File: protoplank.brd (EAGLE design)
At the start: 80 x 49 mm, 110 parts, among them IC1 74AHC1G86DBV

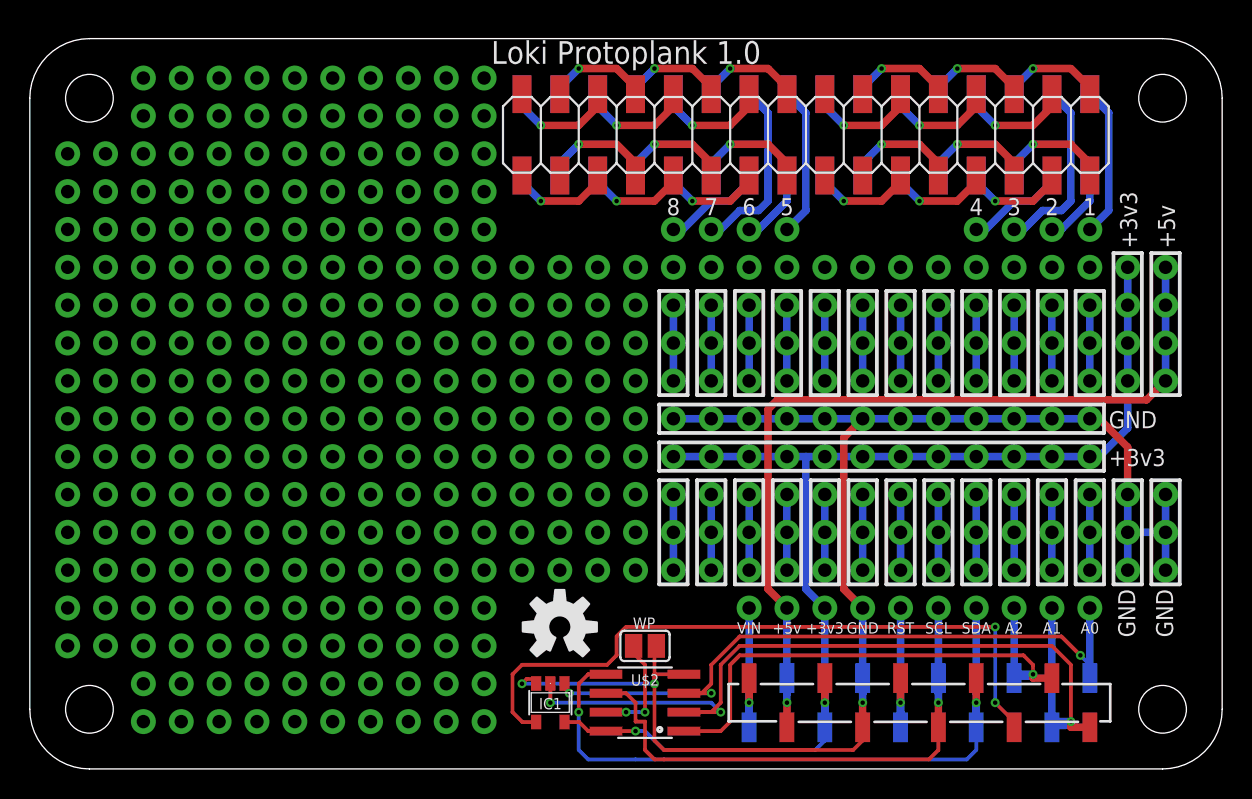
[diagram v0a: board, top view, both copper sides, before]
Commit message: Updated protoplank to use square pads for ease of SMT soldering.
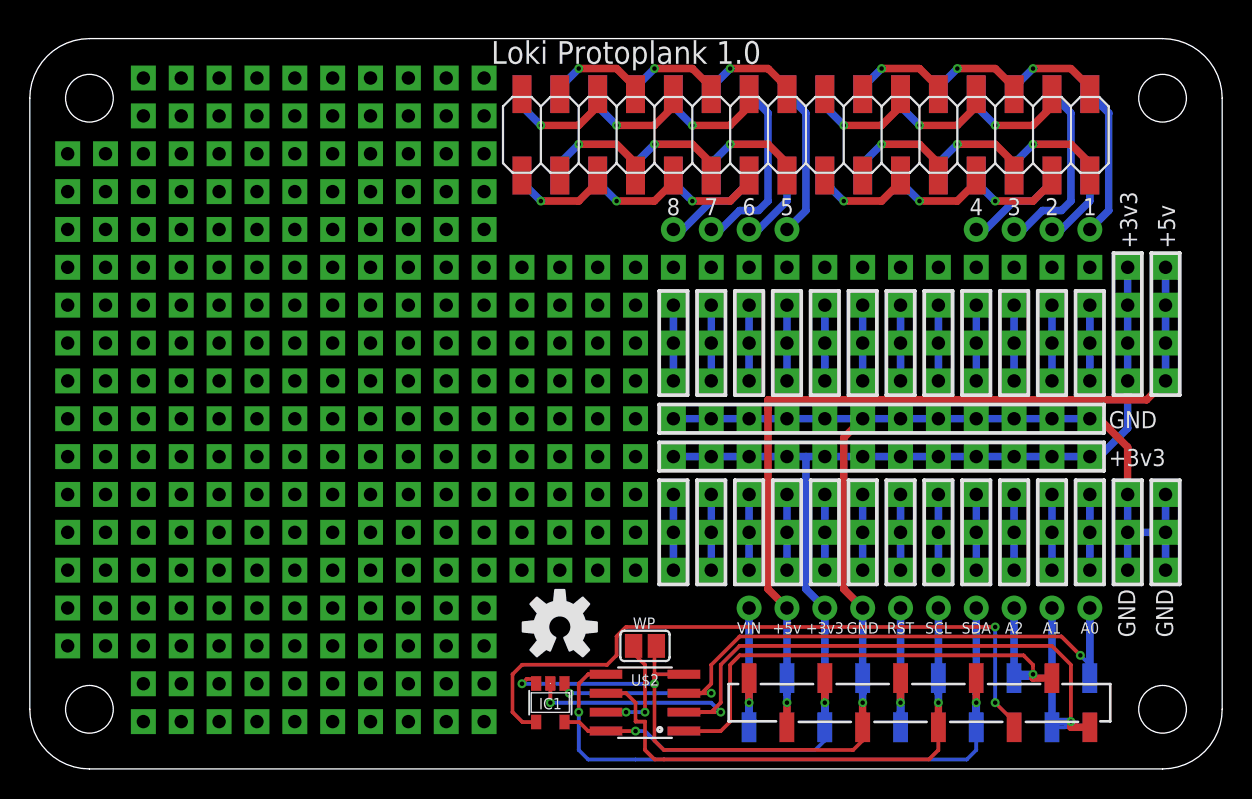
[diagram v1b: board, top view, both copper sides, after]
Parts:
- U$100, U$101, U$102, U$103, U$23, U$24, U$25, U$26, U$34, U$35, U$36, U$37, U$38, U$39, U$40, U$41, U$42, U$43, U$44, U$45, U$46, U$47, U$48, U$49, U$50, U$51, U$52, U$53, U$54, U$55, U$56, U$57, U$58, U$59, U$60, U$61, U$62, U$63, U$64, U$65, U$66, U$67, U$68, U$69, U$70, U$71, U$72, U$73, U$74, U$75, U$76, U$77, U$79, U$81, U$82, U$83, U$84, U$85, U$86, U$87, U$88, U$89, U$90, U$91, U$92, U$93, U$94, U$95, U$96, U$97, U$98, U$99: value PROTOPAD-4 -> PROTOPAD-4SQUARE
- U$104, U$105, U$106, U$107, U$27, U$28: value PROTOPAD-2 -> PROTOPAD-2SQUARE
- U$29, U$30, U$31, U$32: value PROTOPAD-4 -> PROTOPAD-4ROUND; device nickparts:PROTOPAD-4 -> nickparts:PROTOPAD-4-ROUND
- U$33: value PROTOPAD-2 -> PROTOPAD-2ROUND; device nickparts:PROTOPAD-2 -> nickparts:PROTOPAD-2-ROUND

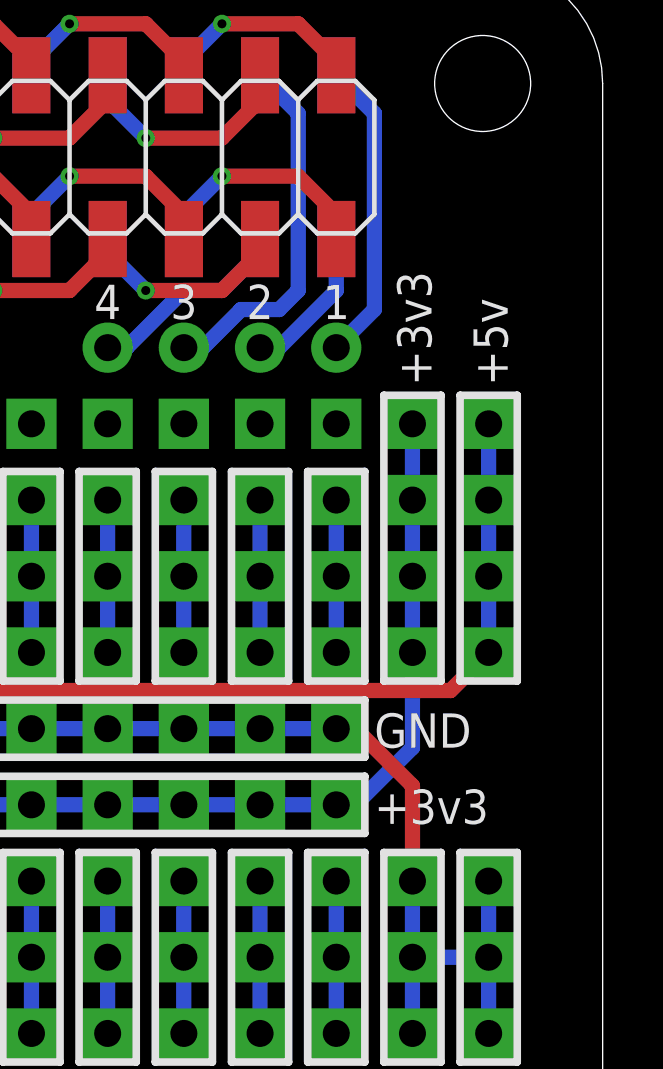
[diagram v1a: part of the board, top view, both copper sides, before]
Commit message: Added decoupling capacitors to the protoboard.
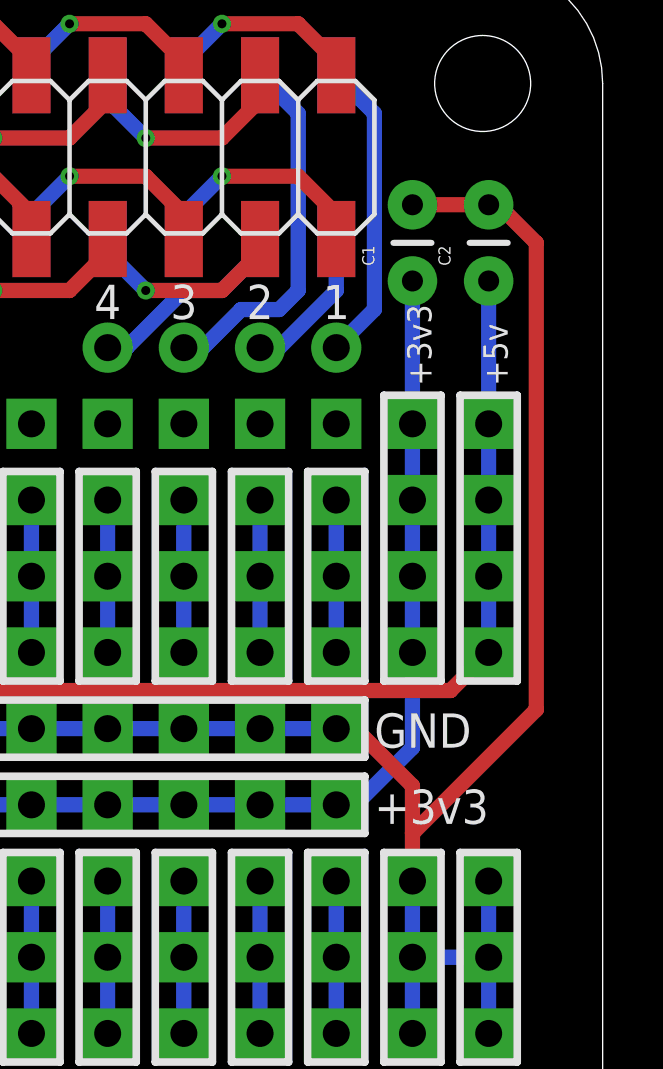
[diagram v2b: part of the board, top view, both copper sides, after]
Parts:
- added C1, C2: (no value), SparkFun-Passives:CAP-PTH-SMALL
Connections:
- net +3V3: now also C1.1
- net +5V: now also C2.1
- net GND: now also C1.2, C2.2
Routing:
- net GND: track 105.3 -> 131.3 mm
- net +3V3: track 82.4 -> 87.2 mm
- net +5V: track 58.3 -> 63.1 mm
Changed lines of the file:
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@@
 <text x="73.66" y="22.86" size="1.143" layer="21">GND</text>
 <text x="73.66" y="20.32" size="1.143" layer="21">+3v3</text>
-<text x="75.565" y="34.925" size="1.143" layer="21" rot="R90">+3v3</text>
-<text x="78.105" y="34.925" size="1.143" layer="21" rot="R90">+5v</text>
+<text x="75.565" y="34.925" size="0.8128" layer="21" rot="R90">+3v3</text>
+<text x="78.105" y="34.925" size="0.8128" layer="21" rot="R90">+5v</text>
 <text x="74.295" y="12.065" size="1.143" layer="21" rot="R270">GND</text>
 <text x="76.835" y="12.065" size="1.143" layer="21" rot="R270">GND</text>
@@
 <element name="U$107" library="nickparts" package="PROTOPAD-2" value="PROTOPAD-2SQUARE" x="8.89" y="45.085"/>
 <element name="U$108" library="SparkFun-Aesthetics" package="OSHW-LOGO-M" value="" x="36.83" y="9.525"/>
+<element name="C1" library="SparkFun-Passives" package="CAP-PTH-SMALL" value="" x="74.93" y="38.4175" rot="R90"/>
+<element name="C2" library="SparkFun-Passives" package="CAP-PTH-SMALL" value="" x="77.47" y="38.4175" rot="R90"/>
 </elements>
 <signals>
@@
 <wire x1="51.435" y1="24.765" x2="50.8" y2="24.765" width="0.508" layer="1"/>
 <wire x1="50.8" y1="24.765" x2="50.8" y2="24.13" width="0.508" layer="1"/>
+<contactref element="C2" pad="1"/>
+<wire x1="77.47" y1="38.4175" x2="77.47" y2="33.655" width="0.508" layer="16"/>
 </signal>
 <signal name="+3V3">
@@
 <wire x1="73.025" y1="20.955" x2="74.93" y2="22.86" width="0.508" layer="16"/>
 <wire x1="74.93" y1="22.86" x2="74.93" y2="26.035" width="0.508" layer="16"/>
+<contactref element="C1" pad="1"/>
+<wire x1="74.93" y1="38.4175" x2="74.93" y2="33.655" width="0.508" layer="16"/>
 </signal>
 <signal name="GND">
@@
 <wire x1="72.39" y1="23.495" x2="73.025" y2="23.495" width="0.508" layer="1"/>
 <wire x1="73.025" y1="23.495" x2="74.93" y2="21.59" width="0.508" layer="1"/>
-<wire x1="74.93" y1="21.59" x2="74.93" y2="18.415" width="0.508" layer="1"/>
+<wire x1="74.93" y1="21.59" x2="74.93" y2="20.0025" width="0.508" layer="1"/>
+<contactref element="C1" pad="2"/>
+<contactref element="C2" pad="2"/>
+<wire x1="74.93" y1="20.0025" x2="74.93" y2="18.415" width="0.508" layer="1"/>
+<wire x1="77.47" y1="40.9575" x2="77.7875" y2="40.9575" width="0.508" layer="1"/>
+<wire x1="77.7875" y1="40.9575" x2="79.0575" y2="39.6875" width="0.508" layer="1"/>
+<wire x1="79.0575" y1="39.6875" x2="79.0575" y2="24.13" width="0.508" layer="1"/>
+<wire x1="79.0575" y1="24.13" x2="74.93" y2="20.0025" width="0.508" layer="1"/>
+<wire x1="77.47" y1="40.9575" x2="74.93" y2="40.9575" width="0.508" layer="1"/>
 </signal>
 <signal name="A0">

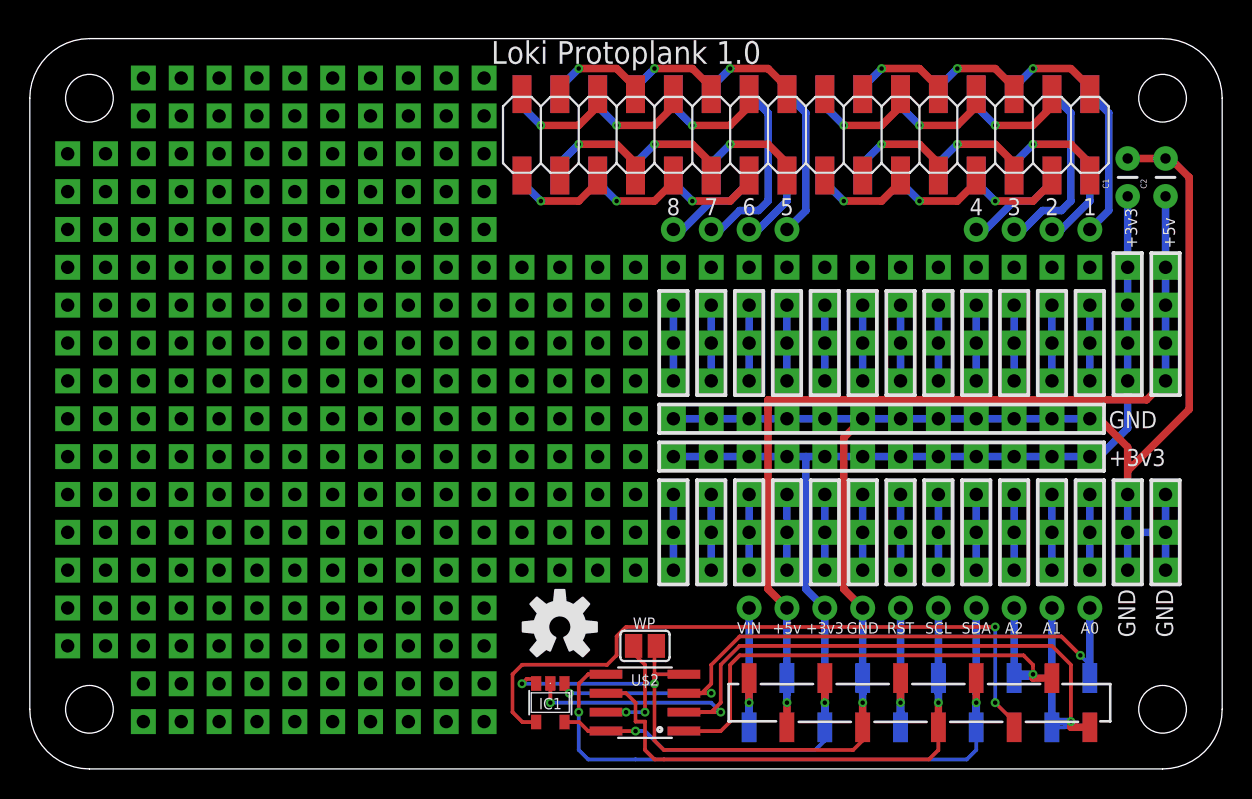
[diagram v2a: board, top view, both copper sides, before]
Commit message: Added tripads for edge connectors on protoshield.
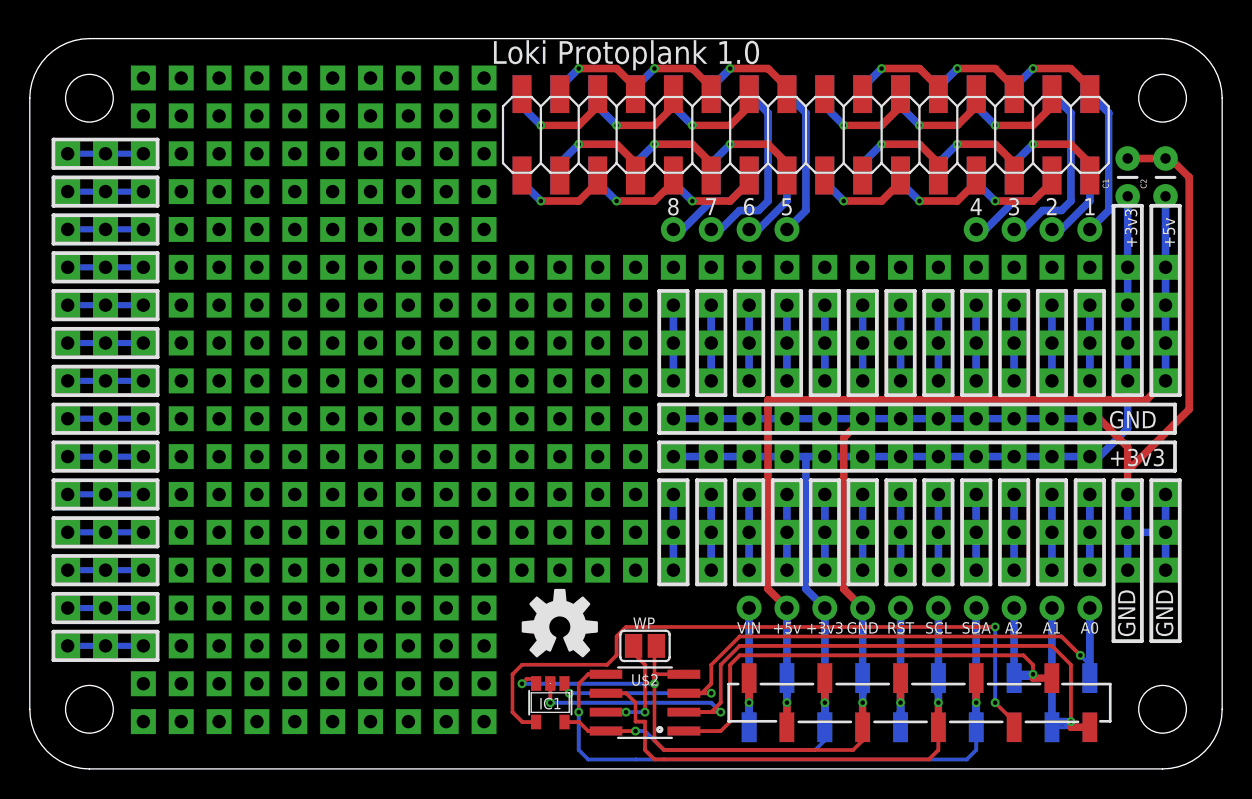
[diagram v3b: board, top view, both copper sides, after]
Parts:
- moved U$93 20.5 mm to (27.9, 5.71)
- moved U$96 20.5 mm to (7.62, 8.26)
- moved U$81 20.3 mm to (7.62, 36.2)
- moved U$83 20.3 mm to (27.9, 36.2)
- moved U$63 16.3 mm to (16.5, 17.1)
- moved U$69 16.3 mm to (3.81, 27.3)
- moved U$58 12.7 mm to (14.0, 17.1)
- moved U$90 12.7 mm to (17.8, 3.17)
- moved U$99 12.7 mm to (7.62, 10.8)
- moved U$59 10.5 mm to (11.4, 17.1)
- moved U$65 10.5 mm to (8.89, 27.3)
- moved U$66 10.5 mm to (6.35, 27.3)
- moved U$84 10.5 mm to (17.8, 41.3)
- moved U$88 10.5 mm to (7.62, 38.7)
- moved U$67 5.08 mm to (6.35, 17.1)
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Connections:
- new net N$54: U$89.P$1, U$89.P$2, U$89.P$3
- new net N$55: U$88.P$1, U$88.P$2, U$88.P$3
- new net N$58: U$81.P$1, U$81.P$2, U$81.P$3
- new net N$61: U$76.P$1, U$76.P$2, U$76.P$3
- new net N$62: U$65.P$1, U$66.P$1, U$69.P$1
- new net N$63: U$65.P$2, U$66.P$2, U$69.P$2
- new net N$64: U$65.P$3, U$66.P$3, U$69.P$3
- new net N$65: U$65.P$4, U$66.P$4, U$69.P$4
- new net N$66: U$64.P$1, U$67.P$1, U$68.P$1
- new net N$67: U$64.P$2, U$67.P$2, U$68.P$2
- new net N$68: U$64.P$3, U$67.P$3, U$68.P$3
- new net N$69: U$64.P$4, U$67.P$4, U$68.P$4
- new net N$70: U$96.P$1, U$96.P$2, U$96.P$3
- new net N$71: U$99.P$1, U$99.P$2, U$99.P$3
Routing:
- net N$71: track 0.00 -> 5.08 mm
- net N$70: track 0.00 -> 5.08 mm
- net N$69: track 0.00 -> 5.08 mm
- net N$68: track 0.00 -> 5.08 mm
- net N$67: track 0.00 -> 5.08 mm
- net N$66: track 0.00 -> 5.08 mm
- net N$65: track 0.00 -> 5.08 mm
- net N$64: track 0.00 -> 5.08 mm
- net N$63: track 0.00 -> 5.08 mm
- net N$62: track 0.00 -> 5.08 mm
- net N$61: track 0.00 -> 5.08 mm
- net N$58: track 0.00 -> 5.08 mm
- net N$55: track 0.00 -> 5.08 mm
- net N$54: track 0.00 -> 5.08 mm
